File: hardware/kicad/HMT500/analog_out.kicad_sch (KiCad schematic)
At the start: 20 parts, among them U10 TPS26611, U7 DAC8760IPWP, U8 DAC8760IPWP, U9 TPS26611

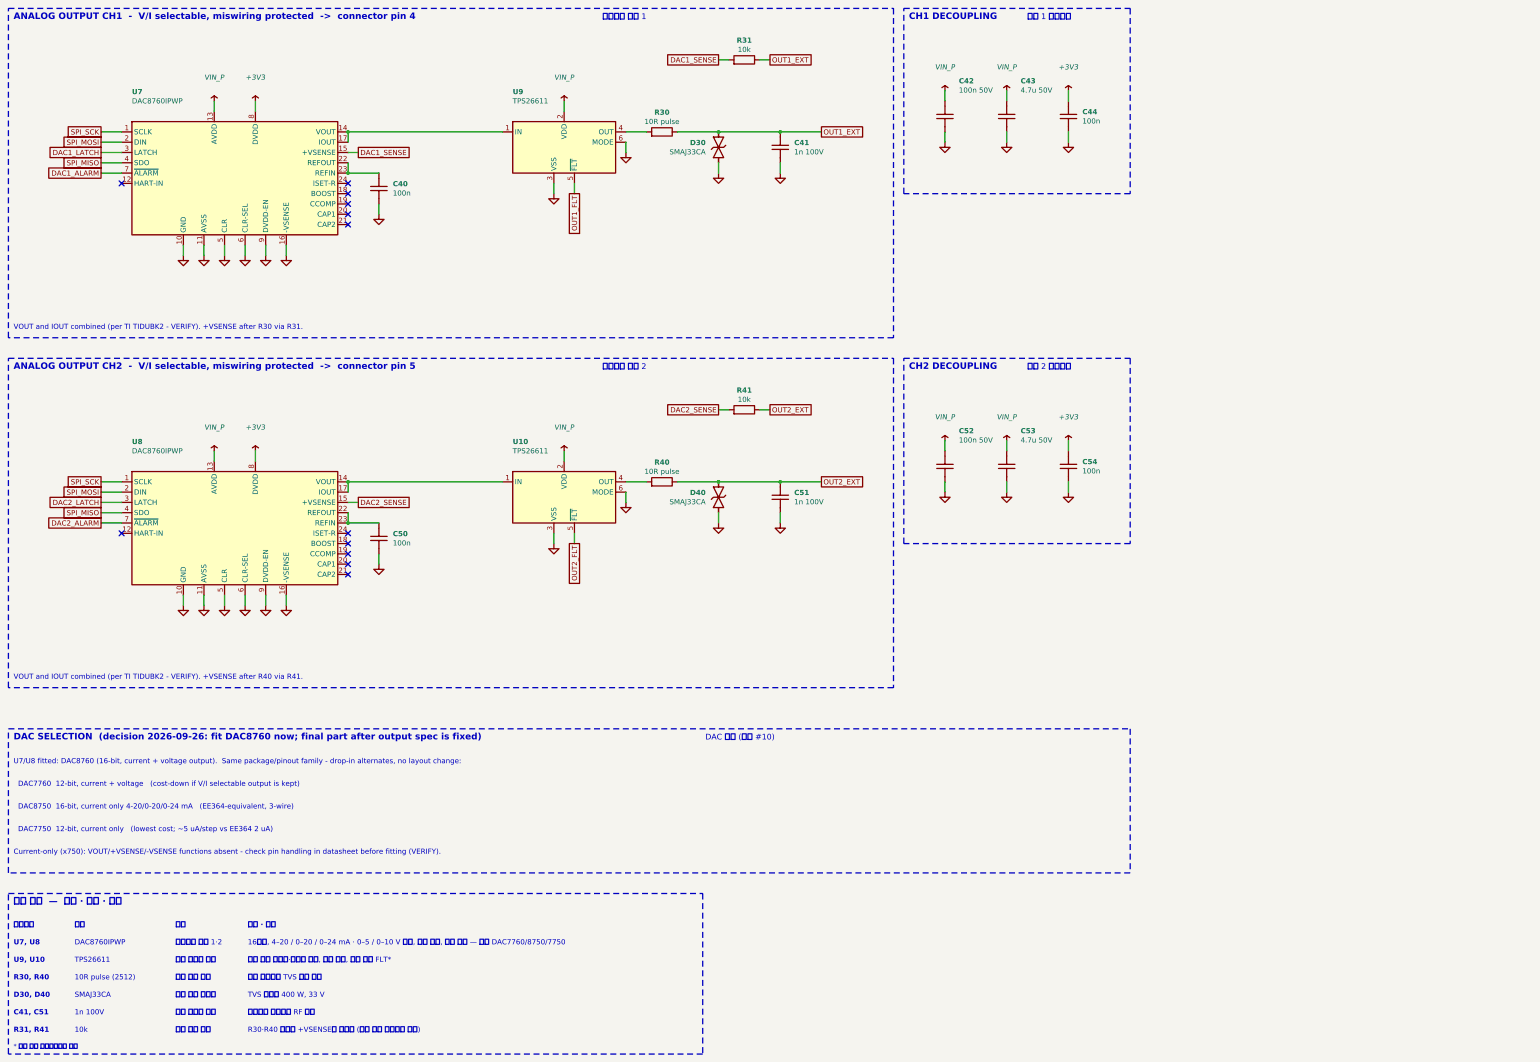
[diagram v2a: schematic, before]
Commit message: Schematic v0.7: DAC8760 real pinout, OPA197 +VSENSE buffer, ISET-R, SPI2 daisy chain
- DAC8760 symbol from datasheet SBAS528D (HTSSOP-24 PWP + EP), same as
  VibrationSensor IVS320; placeholder pins removed, VERIFY flag dropped
- +VSENSE via OPA197 unity-gain follower (U12/U13) of the terminal voltage;
  R31/R41 10k kept as buffer input protection; C45/C55 V+ bypass
- External ISET-R 15k 0.1% 25 ppm (R32/R42)
- DACs on dedicated SPI2 (PB13/14/15) daisy chain with common DAC_LATCH
  (PB10); R33 100k pull-down on DAC_DAISY; ALARM -> PB11/PB3, PWR_FLT -> PB4
- Output protection unification (TPS26611 vs passive) left on hold
- Parts list, circuit-design doc, decision log #24 updated; netlist 70/70, 0 errors

Co-Authored-By: Claude Opus 5.5 <noreply@anthropic.com>
Claude-Session: https://claude.ai/code/session_01JA2o8uJsqp9Vzsg4b665ev
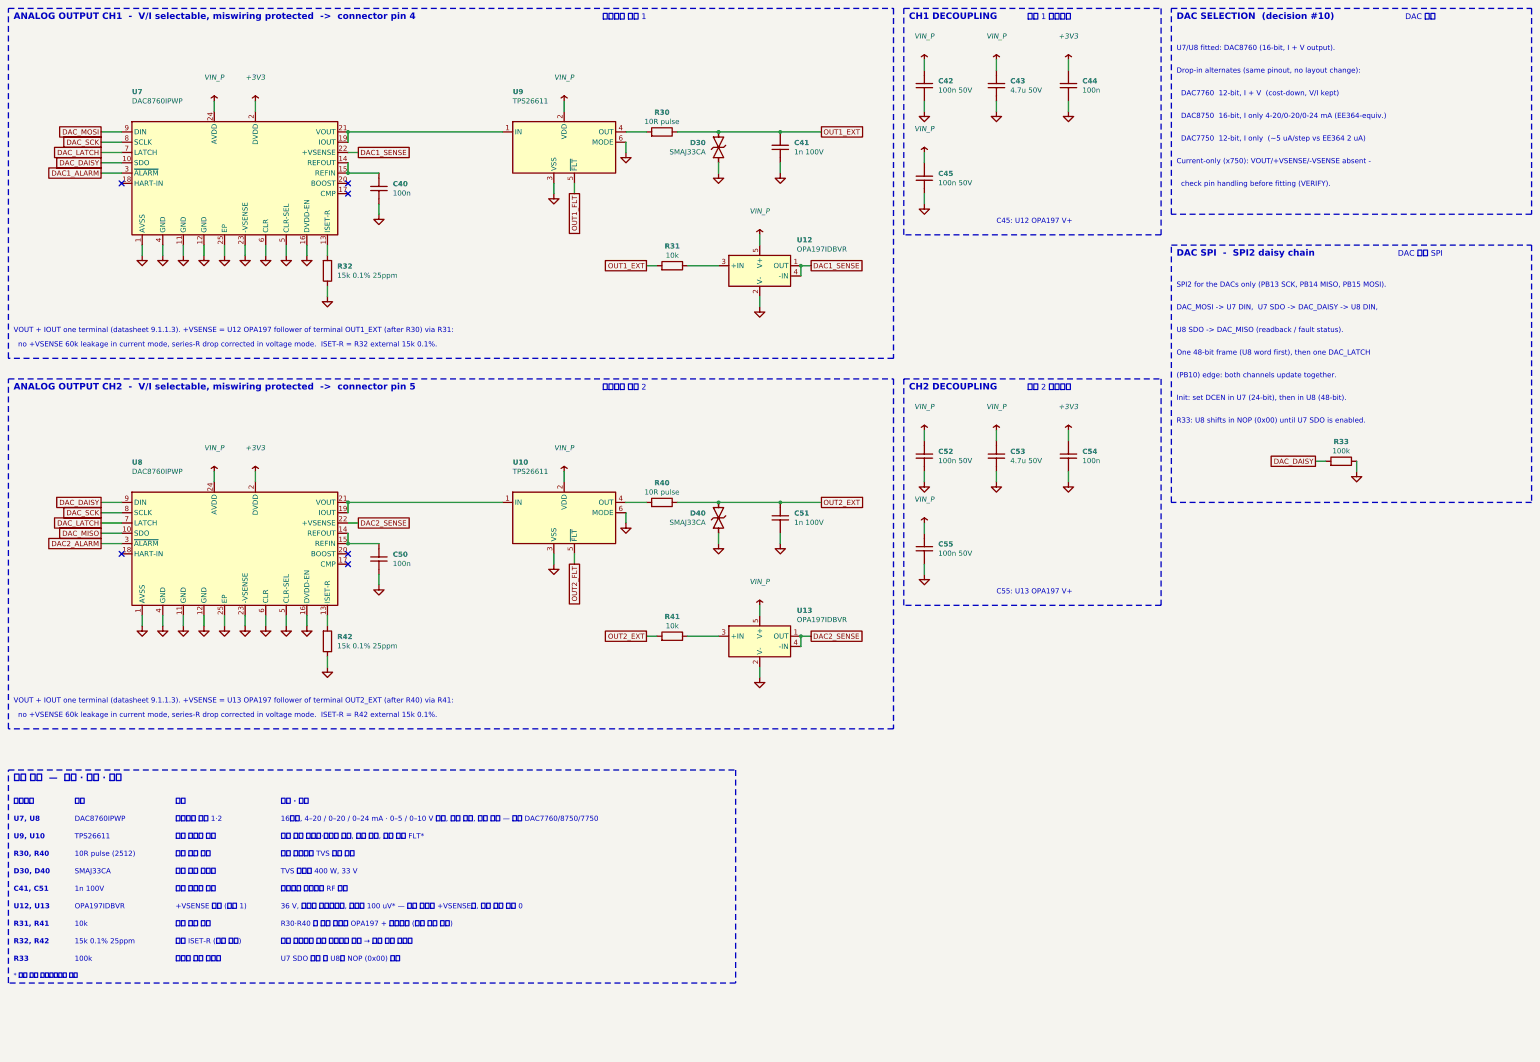
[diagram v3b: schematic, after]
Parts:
- added C45, C55: 100n 50V, Capacitor_SMD:C_0805_2012Metric, symbol HMT500:C
- added R32, R42: 15k 0.1% 25ppm, Resistor_SMD:R_0603_1608Metric, symbol HMT500:R
- added R33: 100k, Resistor_SMD:R_0603_1608Metric, symbol HMT500:R
- added U12, U13: OPA197IDBVR, Package_TO_SOT_SMD:SOT-23-5, symbol HMT500:OPA197
- U7, U8: footprint TBD:HTSSOP-24_DAC8760 -> Package_SO:HTSSOP-24-1EP_4.4x7.8mm_P0.65mm_EP3.2x5mm; VERIFY YES - pin numbers are placeholders -> (none)
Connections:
- net DAC1_LATCH is gone; now on net DAC1_ALARM: U7.3 (~{ALARM})
- net DAC2_LATCH is gone; now on net DAC2_ALARM: U8.3 (~{ALARM})
- net SPI_MISO is gone; now on net GND: U7.4 (GND), U8.4 (GND)
- net SPI_MOSI is gone; now on net +3V3: U7.2 (DVDD), U8.2 (DVDD)
- net SPI_SCK is gone; now on net GND: U7.1 (AVSS), U8.1 (AVSS)
- net +3V3: no longer U7.8 (DVDD), U8.8 (DVDD)
- net DAC1_ALARM: no longer U7.7 (~{ALARM})
- net DAC1_SENSE: now also U7.22 (+VSENSE), U12.1 (OUT), U12.4 (-IN); no longer R31.1, U7.15 (+VSENSE)
- net DAC2_ALARM: no longer U8.7 (~{ALARM})
- net DAC2_SENSE: now also U8.22 (+VSENSE), U13.1 (OUT), U13.4 (-IN); no longer R41.1, U8.15 (+VSENSE)
- net GND: now also U7.12 (GND), U7.23 (-VSENSE), U7.25 (EP), U8.12 (GND), U8.23 (-VSENSE), U8.25 (EP), C45.2, C55.2, R32.2, R33.2, R42.2, U12.2 (V-), U13.2 (V-); no longer U7.10 (GND), U7.9 (DVDD-EN), U8.10 (GND), U8.9 (DVDD-EN)
- net OUT1_EXT: now also R31.1; no longer R31.2
- net OUT2_EXT: now also R41.1; no longer R41.2
- net VIN_P: now also U7.24 (AVDD), U8.24 (AVDD), C45.1, C55.1, U12.5 (V+), U13.5 (V+); no longer U7.13 (AVDD), U8.13 (AVDD)
- net at U7.19 (IOUT): now also U7.21 (VOUT), U9.1 (IN)
- net at U8.19 (IOUT): now also U10.1 (IN), U8.21 (VOUT)
- new net: C40.1, U7.14 (REFOUT), U7.15 (REFIN)
- new net: R32.1, U7.13 (ISET-R)
- new net: R42.1, U8.13 (ISET-R)
- new net: R41.2, U13.3 (+IN)
- new net: C50.1, U8.14 (REFOUT), U8.15 (REFIN)
- new net: R31.2, U12.3 (+IN)
- new net DAC_DAISY: R33.1, U7.10 (SDO), U8.9 (DIN)
- new net DAC_LATCH: U7.7 (LATCH), U8.7 (LATCH)
- new net DAC_MISO: U8.10 (SDO)
- new net DAC_MOSI: U7.9 (DIN)
- new net DAC_SCK: U7.8 (SCLK), U8.8 (SCLK)
- now unconnected: U7.17 (IOUT), U8.17 (IOUT)
- no-connect marks 12 -> 6
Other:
- note added: "(PB10) edge: both channels update together."
- note added: "+VSENSE 버퍼 (이득 1)"
- note added: "100k"
- note added: "15k 0.1% 25ppm"
- note added: "36 V, 입출력 레일투레일, 오프셋 100 uV* — 단자 전압을 +VSENSE로, 전류 모드 누설 0"
- note added: "C45: U12 OPA197 V+"
- note added: "C55: U13 OPA197 V+"
- note added: "Current-only (x750): VOUT/+VSENSE/-VSENSE absent -"
- note added: "DAC SELECTION (decision #10)"
- note added: "DAC SPI - SPI2 daisy chain"
- note added: "DAC 선정"
- note added: "DAC 전용 SPI"
- note added: "DAC7750 12-bit, I only (~5 uA/step vs EE364 2 uA)"
- note added: "DAC7760 12-bit, I + V (cost-down, V/I kept)"
- note added: "DAC8750 16-bit, I only 4-20/0-20/0-24 mA (EE364-equiv.)"
- note added: "DAC_MOSI -> U7 DIN, U7 SDO -> DAC_DAISY -> U8 DIN,"
- note added: "Drop-in alternates (same pinout, no layout change):"
- note added: "Init: set DCEN in U7 (24-bit), then in U8 (48-bit)."
- note added: "OPA197IDBVR"
- note added: "One 48-bit frame (U8 word first), then one DAC_LATCH"
- note added: "R30·R40 뒤 단자 전압을 OPA197 + 입력으로 (서지 전류 제한)"
- note added: "R32, R42"
- note added: "R33"
- note added: "R33: U8 shifts in NOP (0x00) until U7 SDO is enabled."
- note added: "SPI2 for the DACs only (PB13 SCK, PB14 MISO, PB15 MOSI)."
- note added: "U12, U13"
- note added: "U7 SDO 켜기 전 U8에 NOP (0x00) 입력"
- note added: "U7/U8 fitted: DAC8760 (16-bit, I + V output)."
- note added: "U8 SDO -> DAC_MISO (readback / fault status)."
- note added: "VOUT + IOUT one terminal (datasheet 9.1.1.3). +VSENSE = U12 OPA197 follower of terminal OUT1_EXT (after R30) via R31:"
- note added: "VOUT + IOUT one terminal (datasheet 9.1.1.3). +VSENSE = U13 OPA197 follower of terminal OUT2_EXT (after R40) via R41:"
- note added: "check pin handling before fitting (VERIFY)."
- note added: "no +VSENSE 60k leakage in current mode, series-R drop corrected in voltage mode. ISET-R = R32 external 15k 0.1%."
- note added: "no +VSENSE 60k leakage in current mode, series-R drop corrected in voltage mode. ISET-R = R42 external 15k 0.1%."
- note added: "내부 저항보다 온도 드리프트 작음 → 전류 출력 정확도"
- note added: "데이지 체인 풀다운"
- note added: "버퍼 입력 보호"
- note added: "외부 ISET-R (전류 기준)"
- note removed: "Current-only (x750): VOUT/+VSENSE/-VSENSE functions absent - check pin handling in datasheet before fitting (VERIFY)."
- note removed: "DAC SELECTION (decision 2026-09-26: fit DAC8760 now; final part after output spec is fixed)"
- note removed: "DAC 선정 (결정 #10)"
- note removed: "DAC7750 12-bit, current only (lowest cost; ~5 uA/step vs EE364 2 uA)"
- note removed: "DAC7760 12-bit, current + voltage (cost-down if V/I selectable output is kept)"
- note removed: "DAC8750 16-bit, current only 4-20/0-20/0-24 mA (EE364-equivalent, 3-wire)"
- note removed: "R30·R40 뒤에서 +VSENSE로 되먹임 (직렬 저항 전압강하 보상)"
- note removed: "U7/U8 fitted: DAC8760 (16-bit, current + voltage output). Same package/pinout family - drop-in alternates, no layout change:"
- note removed: "VOUT and IOUT combined (per TI TIDUBK2 - VERIFY). +VSENSE after R30 via R31."
- note removed: "VOUT and IOUT combined (per TI TIDUBK2 - VERIFY). +VSENSE after R40 via R41."
- note removed: "전압 출력 감지"
- moved on the sheet: C42, C43, C44, C50, C51, C52, C53, C54, D40, R31, R40, R41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
